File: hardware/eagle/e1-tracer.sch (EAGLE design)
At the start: 118 parts, among them IC1 MCP1703T-1202E/CB, IC2 W25Q80DVSNIG, IC3 TLV70233DBVR, IC4 ASEM1-12.000MHZ-LC-T, J1 PASSTHROUGH, M1 MENTOR_12701001, M2 MENTOR_12701001, SW1 TACTSW-TL3340, T1 BC847C, T2 BC847C, U1 ICE40UP5K-SG48I, U2 IP4234CZ6, U3 IP4234CZ6, U4 IDT82V2081, U5 IDT82V2081, U6 2.048 Mhz, U7 1.544 MHz, X1 MINI-USB-SHIELD-UX60-MB-5ST, X2 JACK2.5_SJ-2523

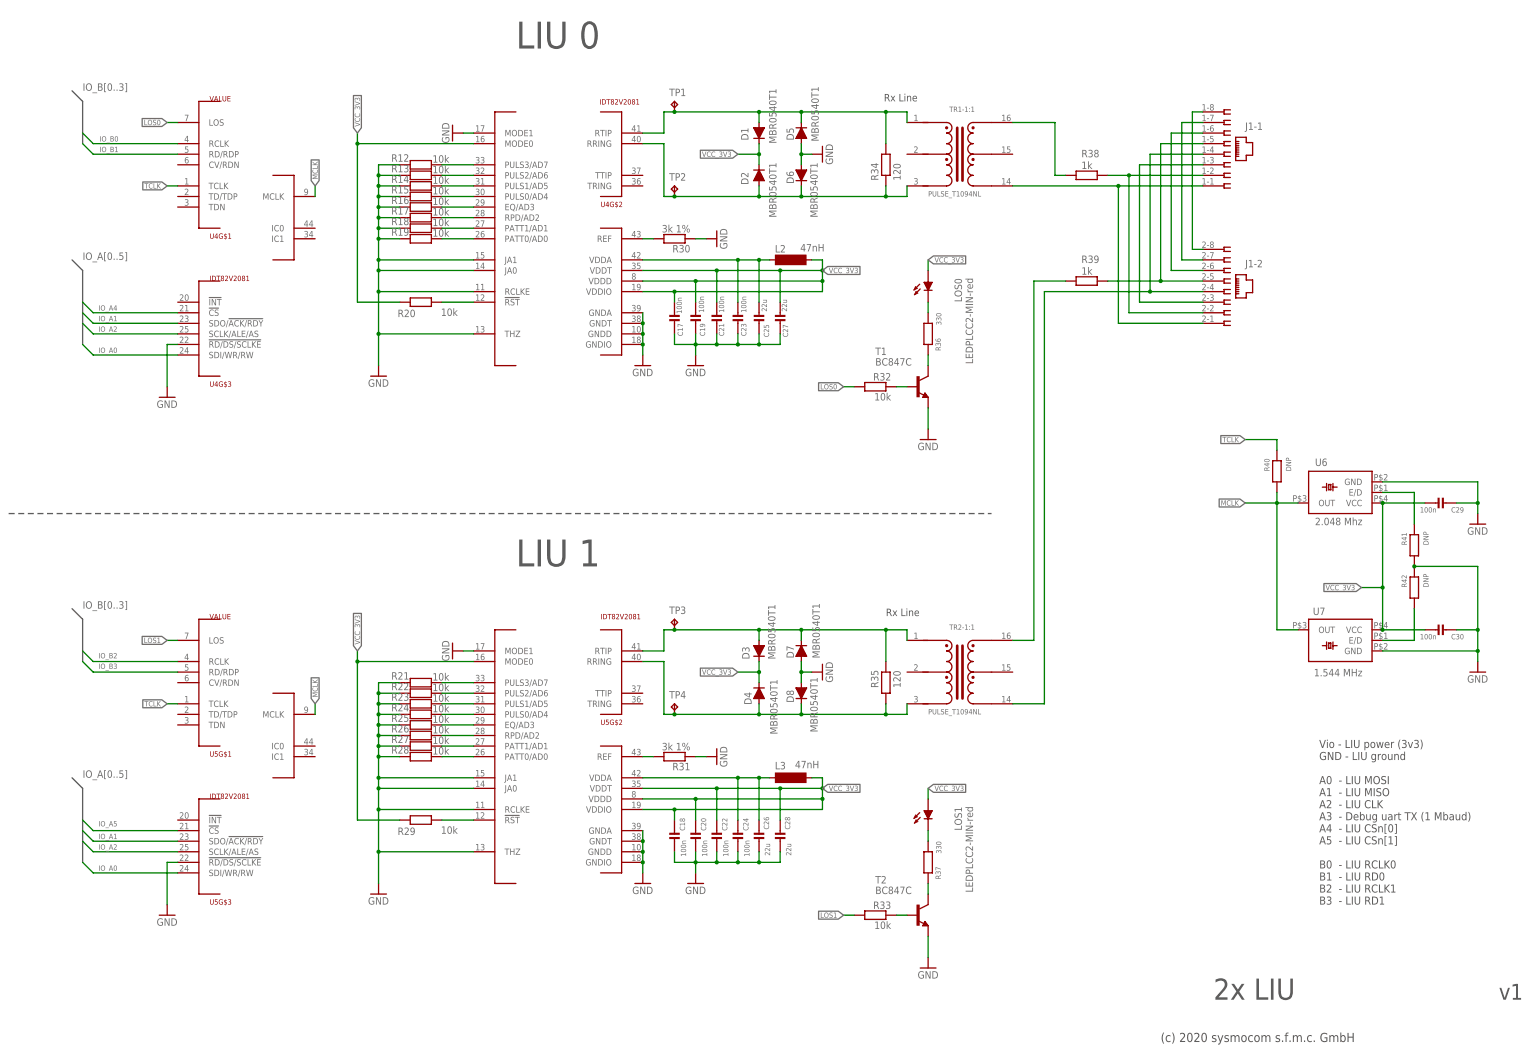
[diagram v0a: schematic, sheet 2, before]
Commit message: e1-tracer: start a last renumber (after inserting 4x 0R)
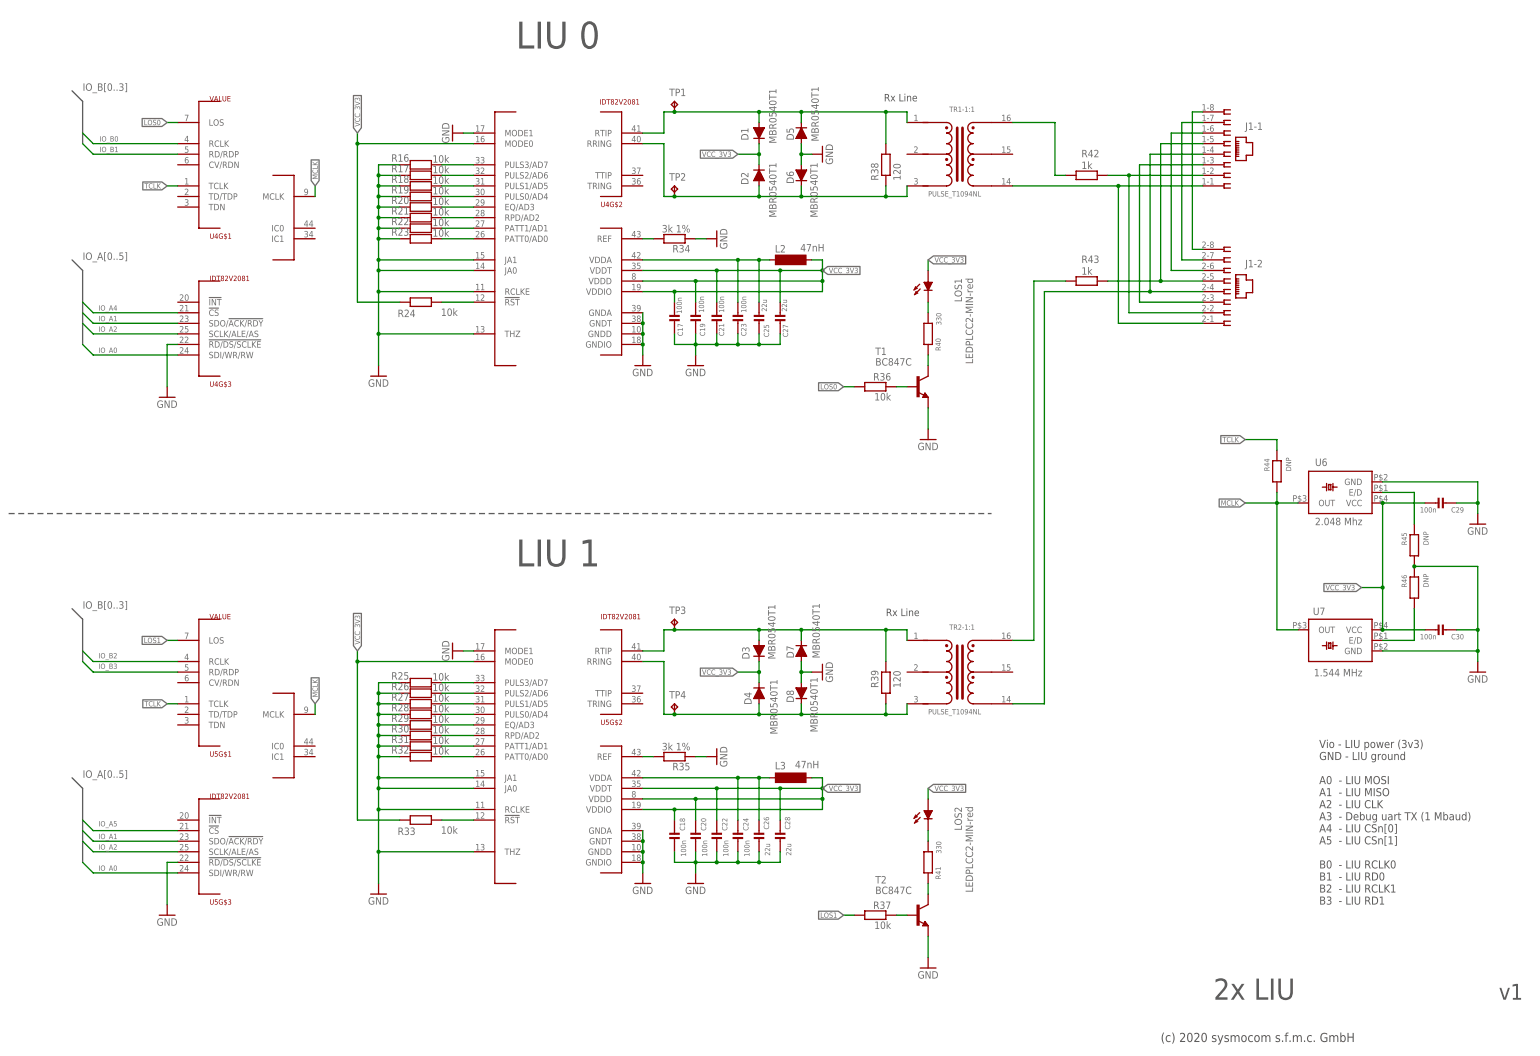
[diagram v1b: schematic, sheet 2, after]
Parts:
- removed LOS0: LEDPLCC2-MIN-red, LED-PLCC2:LEDPLCC2-MIN
- added LOS2: LEDPLCC2-MIN-red, LED-PLCC2:LEDPLCC2-MIN
- C11: value 22u -> 100n; device rc-sysmocom:CAP_CERAMIC1206 -> rc-sysmocom:CAP_CERAMIC_0603; DESCRIPTION CAP CER 22UF 10V 10% X5R 1206 -> CAP CER 0.1UF 16V 10% X7R 0603; LINK http://www.digikey.de/product-detail/de/foo/1276-1287-1-ND -> http://www.digikey.de/product-detail/de/foo/1276-1005-1-ND; MANUFACTURERPARTNUMBER CL31A226KPHNNNE -> CL10B104KO8NNNC; SOURCEPARTNUMBER 1276-1287-1-ND -> 1276-1005-1-ND
- C13: value 10n -> 22u; device rc-sysmocom:CAP_CERAMIC_0402 -> rc-sysmocom:CAP_CERAMIC1206; DESCRIPTION CAP CER 10000PF 25V X7R 0402 -> CAP CER 22UF 10V 10% X5R 1206; LINK https://www.digikey.de/product-detail/de/samsung-electro-me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 -> http://www.digikey.de/product-detail/de/foo/1276-1287-1-ND; MANUFACTURER Samsung Electro-Mechanics -> Samsung Electro-Mechanics America, Inc; MANUFACTURERPARTNUMBER CL05B103KA5NNNC -> CL31A226KPHNNNE; SOURCEPARTNUMBER 1276-1057-1-ND -> 1276-1287-1-ND
- C14: value 100n -> 10n; device rc-sysmocom:CAP_CERAMIC_0603 -> rc-sysmocom:CAP_CERAMIC_0402; DESCRIPTION CAP CER 0.1UF 16V 10% X7R 0603 -> CAP CER 10000PF 25V X7R 0402; LINK http://www.digikey.de/product-detail/de/foo/1276-1005-1-ND -> https://www.digikey.de/product-detail/de/samsung-electro-me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; MANUFACTURER Samsung Electro-Mechanics America, Inc -> Samsung Electro-Mechanics; MANUFACTURERPARTNUMBER CL10B104KO8NNNC -> CL05B103KA5NNNC; SOURCEPARTNUMBER 1276-1005-1-ND -> 1276-1057-1-ND
- R10: MANUFACTURERPARTNUMBER YPE HTML PUBLIC -> RMCF0603FT10K0; ROHSCERTIFICATE Bleifrei / RoHS3-konform -> UNKNOWN ROHS CERTIFICATE
- R11: value 68 -> 100k; DESCRIPTION NO DESCRIPTION -> RES SMD 100K OHM 5%% 1/10W 0603; LINK UNKNOWN LINK -> https://www.digikey.de/product-detail/de/yageo/RC0603JR-071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; MANUFACTURER UNKNOWN MANUFACTURER -> Yageo; MANUFACTURERPARTNUMBER UNKNOWN MANUFACTURER PART NUMBER -> RC0603JR-07100KL; ROHSCERTIFICATE UNKNOWN ROHS CERTIFICATE -> Bleifrei / RoHS-konform; SOURCE UNKNOWN SOURCE -> DIGIKEY; SOURCEPARTNUMBER UNKNOWN SOURCE PART NUMBER -> 311-100KGRCT-ND
- R12: value 10k -> 100k; DESCRIPTION NO DESCRIPTION -> RES SMD 100K OHM 5%% 1/10W 0603; LINK UNKNOWN LINK -> https://www.digikey.de/product-detail/de/yageo/RC0603JR-071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; MANUFACTURER UNKNOWN MANUFACTURER -> Yageo; MANUFACTURERPARTNUMBER UNKNOWN MANUFACTURER PART NUMBER -> RC0603JR-07100KL; ROHSCERTIFICATE UNKNOWN ROHS CERTIFICATE -> Bleifrei / RoHS-konform; SOURCE UNKNOWN SOURCE -> DIGIKEY; SOURCEPARTNUMBER UNKNOWN SOURCE PART NUMBER -> 311-100KGRCT-ND
- R13: DESCRIPTION NO DESCRIPTION -> RES 10K OHM 1%% 1/10W 0603; LINK UNKNOWN LINK -> https://www.digikey.de/product-detail/de/stackpole-electron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; MANUFACTURER UNKNOWN MANUFACTURER -> Stackpole Electronics Inc; MANUFACTURERPARTNUMBER UNKNOWN MANUFACTURER PART NUMBER -> YPE HTML PUBLIC; ROHSCERTIFICATE UNKNOWN ROHS CERTIFICATE -> Bleifrei / RoHS3-konform; SOURCE UNKNOWN SOURCE -> DIGIKEY; SOURCEPARTNUMBER UNKNOWN SOURCE PART NUMBER -> RMCF0603FT10K0CT-ND
- R14: value 10k -> 2.2k
- R15: value 10k -> 68
- R2, R3: value 33 -> DNP; device rc-sysmocom:RESISTOR_0402 -> rc-sysmocom:RESISTOR_0603; DESCRIPTION NO DESCRIPTION -> RES SMD 0 OHM JUMPER 1/10W 0603; LINK UNKNOWN LINK -> https://www.digikey.de/product-detail/de/panasonic-electron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; MANUFACTURER UNKNOWN MANUFACTURER -> Panasonic Electronic Components; MANUFACTURERPARTNUMBER UNKNOWN MANUFACTURER PART NUMBER -> ERJ-3GEY0R00V; SOURCE UNKNOWN SOURCE -> DIGIKEY; SOURCEPARTNUMBER UNKNOWN SOURCE PART NUMBER -> P0.0GCT-ND
- R30, R31: value 3k 1% -> 10k
- R34, R35: value 120 -> 3k 1%
- R36, R37: value 330 -> 10k; DESCRIPTION RES SMD 330 OHM 1%% 1/10W 0603 -> NO DESCRIPTION; LINK https://www.digikey.de/product-detail/de/yageo/RC0603FR-073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 -> UNKNOWN LINK; MANUFACTURER Yageo -> UNKNOWN MANUFACTURER; MANUFACTURERPARTNUMBER RC0603FR-07330RL -> UNKNOWN MANUFACTURER PART NUMBER; SOURCE DIGIKEY -> UNKNOWN SOURCE; SOURCEPARTNUMBER 311-330HRCT-ND -> UNKNOWN SOURCE PART NUMBER
- R38, R39: value 1k -> 120
- R4: value 1k5 -> DNP; DESCRIPTION NO DESCRIPTION -> RES SMD 0 OHM JUMPER 1/10W 0603; LINK UNKNOWN LINK -> https://www.digikey.de/product-detail/de/panasonic-electron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; MANUFACTURER UNKNOWN MANUFACTURER -> Panasonic Electronic Components; MANUFACTURERPARTNUMBER UNKNOWN MANUFACTURER PART NUMBER -> ERJ-3GEY0R00V; SOURCE UNKNOWN SOURCE -> DIGIKEY; SOURCEPARTNUMBER UNKNOWN SOURCE PART NUMBER -> P0.0GCT-ND
- R40, R41: value DNP -> 330; DESCRIPTION RES SMD 0 OHM JUMPER 1/10W 0603 -> RES SMD 330 OHM 1%% 1/10W 0603; LINK https://www.digikey.de/product-detail/de/panasonic-electron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 -> https://www.digikey.de/product-detail/de/yageo/RC0603FR-073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; MANUFACTURER Panasonic Electronic Components -> Yageo; MANUFACTURERPARTNUMBER ERJ-3GEY0R00V -> RC0603FR-07330RL; SOURCEPARTNUMBER P0.0GCT-ND -> 311-330HRCT-ND
- R42, R43: value DNP -> 1k; DESCRIPTION RES SMD 0 OHM JUMPER 1/10W 0603 -> NO DESCRIPTION; LINK https://www.digikey.de/product-detail/de/panasonic-electron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 -> UNKNOWN LINK; MANUFACTURER Panasonic Electronic Components -> UNKNOWN MANUFACTURER; MANUFACTURERPARTNUMBER ERJ-3GEY0R00V -> UNKNOWN MANUFACTURER PART NUMBER; SOURCE DIGIKEY -> UNKNOWN SOURCE; SOURCEPARTNUMBER P0.0GCT-ND -> UNKNOWN SOURCE PART NUMBER
- R5: value 10k -> DNP; DESCRIPTION RES 10K OHM 1%% 1/10W 0603 -> RES SMD 0 OHM JUMPER 1/10W 0603; LINK https://www.digikey.de/product-detail/de/stackpole-electron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 -> https://www.digikey.de/product-detail/de/panasonic-electron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; MANUFACTURER Stackpole Electronics Inc -> Panasonic Electronic Components; MANUFACTURERPARTNUMBER YPE HTML PUBLIC -> ERJ-3GEY0R00V; ROHSCERTIFICATE Bleifrei / RoHS3-konform -> UNKNOWN ROHS CERTIFICATE; SOURCEPARTNUMBER RMCF0603FT10K0CT-ND -> P0.0GCT-ND
- R6, R7: value 100k -> 33; device rc-sysmocom:RESISTOR_0603 -> rc-sysmocom:RESISTOR_0402; DESCRIPTION RES SMD 100K OHM 5%% 1/10W 0603 -> NO DESCRIPTION; LINK https://www.digikey.de/product-detail/de/yageo/RC0603JR-071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 -> UNKNOWN LINK; MANUFACTURER Yageo -> UNKNOWN MANUFACTURER; MANUFACTURERPARTNUMBER RC0603JR-07100KL -> UNKNOWN MANUFACTURER PART NUMBER; ROHSCERTIFICATE Bleifrei / RoHS-konform -> UNKNOWN ROHS CERTIFICATE; SOURCE DIGIKEY -> UNKNOWN SOURCE; SOURCEPARTNUMBER 311-100KGRCT-ND -> UNKNOWN SOURCE PART NUMBER
- R8: MANUFACTURERPARTNUMBER RMCF0603FT10K0 -> YPE HTML PUBLIC; ROHSCERTIFICATE UNKNOWN ROHS CERTIFICATE -> Bleifrei / RoHS3-konform
- R9: value 2.2k -> 1k5
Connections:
- net CDONE: now also R14.2; no longer R9.2
- net GND: now also R11.1, R20.2, R29.2, R30.2, R31.2, R32.2, R34.1, R35.1, R45.2, R46.1; no longer R11.2, R12.2, R13.2, R14.2, R24.2, R30.1, R31.1, R41.2, R42.1, R6.1
- net IOB_34A_SPI_SCK: now also R10.1; no longer R8.1
- net IOB_35B_SPI_SS: now also R8.1; no longer R5.1
- net LOS0: now also R36.2; no longer R32.2
- net LOS1: now also R37.2; no longer R33.2
- net MCLK: now also R44.2; no longer R40.2
- net N$1: now also R35.2; no longer R31.2
- net N$10: now also R18.1; no longer R14.1
- net N$11: now also R19.1; no longer R15.1
- net N$12: now also R20.1; no longer R16.1
- net N$13: now also R21.1; no longer R17.1
- net N$14: now also R22.1; no longer R18.1
- net N$15: now also R27.1; no longer R23.1
- net N$16: now also R28.1; no longer R24.1
- net N$17: now also R24.1; no longer R20.1
- net N$18: now also R23.1; no longer R19.1
- net N$19: now also R29.1; no longer R25.1
- net N$2: now also R33.1; no longer R29.1
- net N$20: now also R30.1; no longer R26.1
- net N$21: now also R31.1; no longer R27.1
- net N$22: now also R32.1; no longer R28.1
- net N$25: now also R13.1; no longer R10.1
- net N$26: now also R36.1; no longer R32.1
- net N$27: now also LOS1.C, R40.1; no longer LOS0.C, R36.1
- net N$28: now also R40.2; no longer R36.2
- net N$29: now also R15.1; no longer R11.1
- net N$30: now also R42.1; no longer R38.1
- net N$31: now also R37.1; no longer R33.1
- net N$35: now also R45.1; no longer R41.1
- net N$37: now also LOS2.C, R41.1; no longer LOS1.C, R37.1
- net N$38: now also R46.2; no longer R42.2
- net N$39: now also R41.2; no longer R37.2
- net N$4: now also R34.2; no longer R30.2
- net N$41: now also R43.1; no longer R39.1
- net N$42: now also R42.2; no longer R38.2
- net N$45: now also R2.2, R3.1; no longer R45.2, R46.1
- net N$46: now also R3.2, R5.2; no longer R44.2, R46.2
- net N$5: now also R43.2; no longer R39.2
- net N$55: now also R11.2, R12.1; no longer R6.2, R7.1
- net N$6: now also R25.1; no longer R21.1
- net N$61: now also C14.1, R12.2; no longer C13.1, R7.2
- net N$63: now also R4.2, R5.1; no longer R43.2, R44.1
- net N$65: now also R2.1, R4.1; no longer R43.1, R45.1
- net N$7: now also R26.1; no longer R22.1
- net N$8: now also R16.1; no longer R12.1
- net N$9: now also R17.1; no longer R13.1
- net RRING: now also R38.1; no longer R34.1
- net RRING1: now also R39.1; no longer R35.1
- net RTIP: now also R38.2; no longer R34.2
- net RTIP1: now also R39.2; no longer R35.2
- net TCLK: now also R44.1; no longer R40.1
- net USB1_D_P: now also R9.2; no longer R4.2
- net USB_D_N: now also R6.1; no longer R2.1
- net USB_D_P: now also R7.1; no longer R3.1
- net USB_PU: now also R9.1; no longer R4.1
- net VBUS: now also C13.1; no longer C11.1
- net VCC_3V3: now also C11.1, LOS2.A, R13.2, R14.1, R24.2, R33.2; no longer C14.1, LOS0.A, R20.2, R29.2, R5.2, R9.1
- net _D_N: now also R6.2; no longer R2.2
- net _D_P: now also R7.2; no longer R3.2
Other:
- moved on the sheet: C11, C13, C14, LOS1, R10, R11, R16, R17, R18, R19, R2, R20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
